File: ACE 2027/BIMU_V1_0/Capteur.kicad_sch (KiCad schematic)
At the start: 7 parts, among them J301 Thermal_ResistanceM, U301 LSM6DS3

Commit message: finalisation des connexions pour le BIMU. Il reste encore une révision à faire
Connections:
- no-connect marks 0 -> 1
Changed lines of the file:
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@@
 		(color 0 0 0 0)
+	)
+	(no_connect
+		(at 110.49 157.48)
 	)
 	(wire

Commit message: Finalisé la révision du schéma
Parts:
- removed J301: Thermal_ResistanceM, Connector_PinHeader_1.27mm:PinHeader_1x02_P1.27mm_Vertical, symbol Connector_Generic:Conn_01x02
- removed R301: 10KΩ, Resistor_SMD:R_0805_2012Metric_Pad1.20x1.40mm_HandSolder, symbol Device:R_US
- removed R302, R303: 1.2KΩ, Resistor_SMD:R_0603_1608Metric_Pad0.98x0.95mm_HandSolder, symbol Device:R_US
- C301, C302: footprint Capacitor_SMD:C_0603_1608Metric_Pad1.08x0.95mm_HandSolder -> Capacitor_SMD:C_0805_2012Metric_Pad1.18x1.45mm_HandSolder; Digi-Key_PN 1276-6840-1-ND -> 399-C0805C104K5RACTUCT-ND
- U301: Digi-Key_PN (none) -> 497-LSM6DSV16BXTRCT-ND; Link (none) -> https://www.digikey.ca/en/products/detail/stmicroelectronic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
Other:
- note removed: "THERMALS SENSORS"

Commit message: Réglé les problèmes soulevé par la pull request
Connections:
- net GND: no longer U301.1 (SDO/SA0)
- net SDX: no longer names the net of U301.2 (SDX)
- new net SDO: U301.1 (SDO/SA0)
- no-connect marks 1 -> 2
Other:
- note added: "IMU"
- moved on the sheet: C301, C302, U301

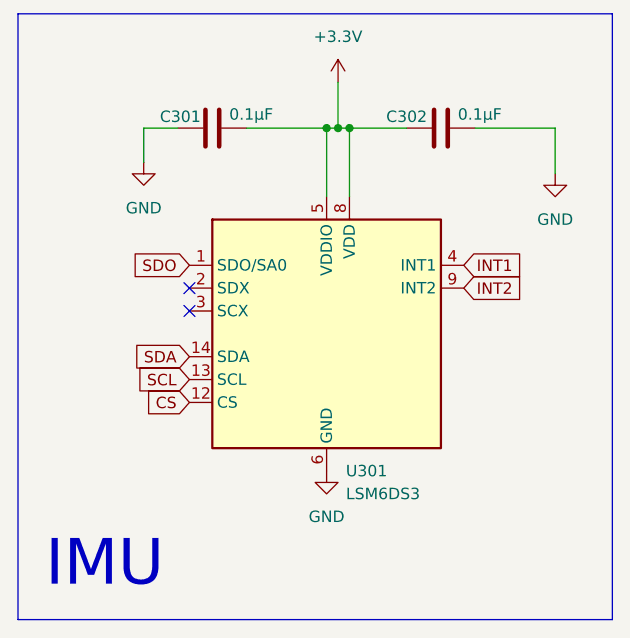
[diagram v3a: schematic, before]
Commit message: Réglé des petits problèmes avec la puce IMU
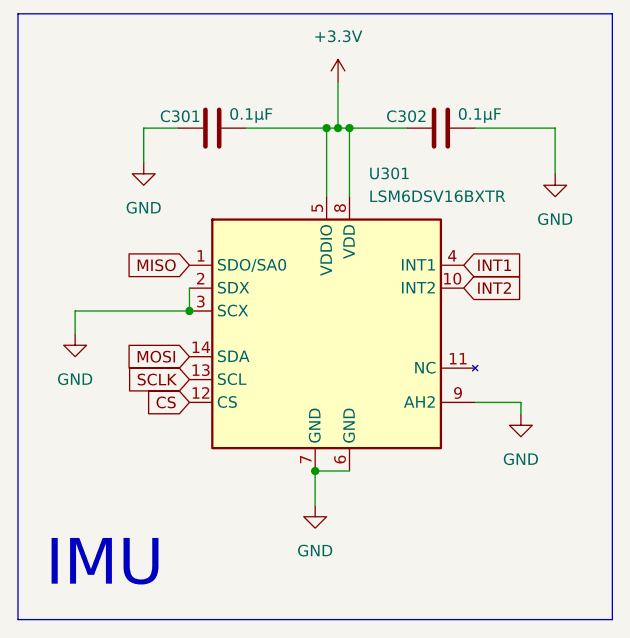
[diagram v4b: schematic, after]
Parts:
- removed U301: LSM6DS3, Package_LGA:LGA-14_3x2.5mm_P0.5mm_LayoutBorder3x4y, symbol Sensor_Motion:LSM6DS3
- added U301: LSM6DSV16BXTR, Package_LGA:LGA-14_3x2.5mm_P0.5mm_LayoutBorder3x4y, symbol BIMU_Custom:LSM6DSV16BXTR
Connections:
- net +3.3V: now also U301.5 (VDDIO), U301.8 (VDD)
- net CS: now also U301.12 (CS)
- net GND: now also U301.2 (SDX), U301.3 (SCX), U301.6 (GND), U301.7 (GND), U301.9 (AH2)
- net INT1: now also U301.4 (INT1)
- net INT2: now also U301.10 (INT2)
- new net MISO: U301.1 (SDO/SA0)
- new net MOSI: U301.14 (SDA)
- new net SCLK: U301.13 (SCL)
- no-connect marks 2 -> 0
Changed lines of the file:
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@@
+	)
+	(junction
+		(at 48.26 67.31)
+		(diameter 0)
+		(color 0 0 0 0)
+	)
+	(junction
+		(at 34.29 49.53)
+		(diameter 0)
+		(color 0 0 0 0)
 	)
 	(junction
@@
 		(color 0 0 0 0)
 	)
-	(no_connect
-		(at 34.29 46.99)
-	)
-	(no_connect
-		(at 34.29 49.53)
+	(wire
+		(pts
+			(xy 71.12 59.69) (xy 71.12 60.96)
+		)
+		(stroke
+			(width 0)
+			(type default)
+		)
+	)
+	(wire
+		(pts
+			(xy 48.26 71.12) (xy 48.26 67.31)
+		)
+		(stroke
+			(width 0)
+			(type default)
+		)
+	)
+	(wire
+		(pts
+			(xy 21.59 49.53) (xy 21.59 52.07)
+		)
+		(stroke
+			(width 0)
+			(type default)
+		)
 	)
 	(wire
@@
 	(wire
 		(pts
+			(xy 34.29 49.53) (xy 21.59 49.53)
+		)
+		(stroke
+			(width 0)
+			(type default)
+		)
+	)
+	(wire
+		(pts
 			(xy 50.8 29.21) (xy 52.07 29.21)
 		)
@@
 	(wire
 		(pts
+			(xy 66.04 59.69) (xy 71.12 59.69)
+		)
+		(stroke
+			(width 0)
+			(type default)
+		)
+	)
+	(wire
+		(pts
 			(xy 52.07 29.21) (xy 58.42 29.21)
 		)
@@
 	(wire
 		(pts
+			(xy 48.26 67.31) (xy 52.07 67.31)
+		)
+		(stroke
+			(width 0)
+			(type default)
+		)
+	)
+	(wire
+		(pts
+			(xy 34.29 46.99) (xy 34.29 49.53)
+		)
+		(stroke
+			(width 0)
+			(type default)
+		)
+	)
+	(wire
+		(pts
 			(xy 52.07 29.21) (xy 52.07 36.83)
 		)
@@
 		)
 	)
-	(global_label "SDO"
+	(global_label "MISO"
 		(shape input)
 		(at 34.29 44.45 180)
@@
 		)
 		(property "Intersheetrefs" "${INTERSHEET_REFS}"
-			(at 27.4948 44.45 0)
+			(at 26.7086 44.45 0)
 			(effects
 				(font
@@
 		)
 	)
-	(global_label "SCL"
+	(global_label "SCLK"
 		(shape input)
 		(at 34.29 57.15 180)
@@
 		)
 		(property "Intersheetrefs" "${INTERSHEET_REFS}"
-			(at 27.7972 57.15 0)
+			(at 26.5272 57.15 0)
 			(effects
 				(font
@@
 		)
 	)
-	(global_label "SDA"
+	(global_label "MOSI"
 		(shape input)
 		(at 34.29 54.61 180)
@@
 		)
 		(property "Intersheetrefs" "${INTERSHEET_REFS}"
-			(at 27.7367 54.61 0)
+			(at 26.7086 54.61 0)
 			(effects
 				(font
@@
 	)
 	(symbol
-		(lib_id "Sensor_Motion:LSM6DS3")
+		(lib_id "BIMU_Custom:LSM6DSV16BXTR")
 		(at 49.53 52.07 0)
 		(unit 1)
@@
 		(fields_autoplaced yes)
 		(property "Reference" "U301"
-			(at 51.6733 67.31 0)
+			(at 54.2133 34.29 0)
 			(effects
 				(font
@@
 			)
 		)
-		(property "Value" "LSM6DS3"
-			(at 51.6733 69.85 0)
+		(property "Value" "LSM6DSV16BXTR"
+			(at 54.2133 36.83 0)
 			(effects
 				(font
@@
 			)
 		)
-		(property "Datasheet" "https://www.st.com/resource/en/datasheet/lsm6ds3tr-c.pdf"
+		(property "Datasheet" "https://www.st.com/content/ccc/resource/technical/document/datasheet/group3/fe/cf/21/3f/ed/a7/43/1c/DM00803257/files/DM00803257.pdf/jcr:content/translations/en.DM00803257.pdf"
 			(at 52.07 68.58 0)
 			(effects
@@
 			)
 		)
-		(property "Link" "https://www.digikey.ca/en/products/detail/stmicroelectronics/LSM6DSV16BXTR/16841542?gclsrc=aw.ds&gad_source=1&gad_campaignid=136320905&gbraid=0AAAAADrbLliJ0xeX3qZwvpkPionXkPT3T&gclid=Cj0KCQjw_7PRBhDcARIsAMjV7jlFHbLXpfjtRcMhcreBAaBLre-3gOjqHCYy_2w3KjlBVbI-xRrxiK4aAsUXEALw_wcB"
+		(property "Link" "https://www.st.com/content/ccc/resource/technical/document/datasheet/group3/fe/cf/21/3f/ed/a7/43/1c/DM00803257/files/DM00803257.pdf/jcr:content/translations/en.DM00803257.pdf"
 			(at 49.53 52.07 0)
 			(effects
@@
 			)
 		)
+		(pin "13"
+		)
+		(pin "12"
+		)
+		(pin "8"
+		)
 		(pin "14"
 		)
+		(pin "5"
+		)
+		(pin "6"
+		)
+		(pin "1"
+		)
+		(pin "7"
+		)
 		(pin "2"
 		)
+		(pin "3"
+		)
+		(pin "4"
+		)
 		(pin "11"
 		)
-		(pin "12"
-		)
-		(pin "13"
-		)
-		(pin "6"
-		)
-		(pin "5"
-		)
-		(pin "1"
-		)
-		(pin "8"
+		(pin "9"
 		)
 		(pin "10"
 		)
-		(pin "4"
-		)
-		(pin "9"
-		)
-		(pin "7"
-		)
-		(pin "3"
-		)
 		(instances
-			(project "BIMU_V_1"
+			(project ""
 				(path "/abeb93ed-b9ef-4503-99a7-3fce380ff294/fb2c5cc6-e994-4380-96ca-0af61efa0b8a"
 					(reference "U301")
@@
 		(dnp no)
 		(fields_autoplaced yes)
-		(property "Reference" "#PWR0303"
+		(property "Reference" "#PWR0304"
 			(at 50.8 27.94 0)
 			(effects
@@
 			(project ""
 				(path "/abeb93ed-b9ef-4503-99a7-3fce380ff294/fb2c5cc6-e994-4380-96ca-0af61efa0b8a"
-					(reference "#PWR0303")
+					(reference "#PWR0304")
+					(unit 1)
+				)
+			)
+		)
+	)
+	(symbol
+		(lib_id "power:GND")
+		(at 21.59 52.07 0)
+		(unit 1)
+		(exclude_from_sim no)
+		(in_bom yes)
+		(on_board yes)
+		(dnp no)
+		(fields_autoplaced yes)
+		(property "Reference" "#PWR0301"
+			(at 21.59 58.42 0)
+			(effects
+				(font
+					(size 1.27 1.27)
+				)
+				(hide yes)
+			)
+		)
+		(property "Value" "GND"
+			(at 21.59 57.15 0)
+			(effects
+				(font
+					(size 1.27 1.27)
+				)
+			)
+		)
+		(property "Footprint" ""
+			(at 21.59 52.07 0)
+			(effects
+				(font
+					(size 1.27 1.27)
+				)
+				(hide yes)
+			)
+		)
+		(property "Datasheet" ""
+			(at 21.59 52.07 0)
+			(effects
+				(font
+					(size 1.27 1.27)
+				)
+				(hide yes)
+			)
+		)
+		(property "Description" "Power symbol creates a global label with name \"GND\" , ground"
+			(at 21.59 52.07 0)
+			(effects
+				(font
+					(size 1.27 1.27)
+				)
+				(hide yes)
+			)
+		)
+		(pin "1"
+		)
+		(instances
+			(project "BIMU_V_1"
+				(path "/abeb93ed-b9ef-4503-99a7-3fce380ff294/fb2c5cc6-e994-4380-96ca-0af61efa0b8a"
+					(reference "#PWR0301")
+					(unit 1)
+				)
+			)
+		)
+	)
+	(symbol
+		(lib_id "power:GND")
+		(at 71.12 60.96 0)
+		(unit 1)
+		(exclude_from_sim no)
+		(in_bom yes)
+		(on_board yes)
+		(dnp no)
+		(fields_autoplaced yes)
+		(property "Reference" "#PWR0305"
+			(at 71.12 67.31 0)
+			(effects
+				(font
+					(size 1.27 1.27)
+				)
+				(hide yes)
+			)
+		)
+		(property "Value" "GND"
+			(at 71.12 66.04 0)
+			(effects
+				(font
+					(size 1.27 1.27)
+				)
+			)
+		)
+		(property "Footprint" ""
+			(at 71.12 60.96 0)
+			(effects
+				(font
+					(size 1.27 1.27)
+				)
+				(hide yes)
+			)
+		)
+		(property "Datasheet" ""
+			(at 71.12 60.96 0)
+			(effects
+				(font
+					(size 1.27 1.27)
+				)
+				(hide yes)
+			)
+		)
+		(property "Description" "Power symbol creates a global label with name \"GND\" , ground"
+			(at 71.12 60.96 0)
+			(effects
+				(font
+					(size 1.27 1.27)
+				)
+				(hide yes)
+			)
+		)
+		(pin "1"
+		)
+		(instances
+			(project "BIMU_V_1"
+				(path "/abeb93ed-b9ef-4503-99a7-3fce380ff294/fb2c5cc6-e994-4380-96ca-0af61efa0b8a"
+					(reference "#PWR0305")
 					(unit 1)
 				)
@@
 		(dnp no)
 		(fields_autoplaced yes)
-		(property "Reference" "#PWR0301"
+		(property "Reference" "#PWR0302"
 			(at 29.21 39.37 0)
 			(effects
@@
 			(project "BIMU_V_1"
 				(path "/abeb93ed-b9ef-4503-99a7-3fce380ff294/fb2c5cc6-e994-4380-96ca-0af61efa0b8a"
-					(reference "#PWR0301")
+					(reference "#PWR0302")
 					(unit 1)
 				)
@@
 		(dnp no)
 		(fields_autoplaced yes)
-		(property "Reference" "#PWR0304"
+		(property "Reference" "#PWR0306"
 			(at 74.93 40.64 0)
 			(effects
@@
 			(project "BIMU_V_1"
 				(path "/abeb93ed-b9ef-4503-99a7-3fce380ff294/fb2c5cc6-e994-4380-96ca-0af61efa0b8a"
-					(reference "#PWR0304")
+					(reference "#PWR0306")
 					(unit 1)
 				)
@@
 	(symbol
 		(lib_id "power:GND")
-		(at 49.53 67.31 0)
+		(at 48.26 71.12 0)
 		(unit 1)
 		(exclude_from_sim no)
@@
 		(dnp no)
 		(fields_autoplaced yes)
-		(property "Reference" "#PWR0302"
-			(at 49.53 73.66 0)
+		(property "Reference" "#PWR0303"
+			(at 48.26 77.47 0)
 			(effects
 				(font
@@
 		)
 		(property "Value" "GND"
-			(at 49.53 72.39 0)
+			(at 48.26 76.2 0)
 			(effects
 				(font
@@
 		)
 		(property "Footprint" ""
-			(at 49.53 67.31 0)
+			(at 48.26 71.12 0)
 			(effects
 				(font
@@
 		)
 		(property "Datasheet" ""
-			(at 49.53 67.31 0)
+			(at 48.26 71.12 0)
 			(effects
 				(font
@@
 		)
 		(property "Description" "Power symbol creates a global label with name \"GND\" , ground"
-			(at 49.53 67.31 0)
+			(at 48.26 71.12 0)
 			(effects
 				(font
@@
 			(project "BIMU_V_1"
 				(path "/abeb93ed-b9ef-4503-99a7-3fce380ff294/fb2c5cc6-e994-4380-96ca-0af61efa0b8a"
-					(reference "#PWR0302")
+					(reference "#PWR0303")
 					(unit 1)
 				)
